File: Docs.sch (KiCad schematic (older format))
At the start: 0 parts

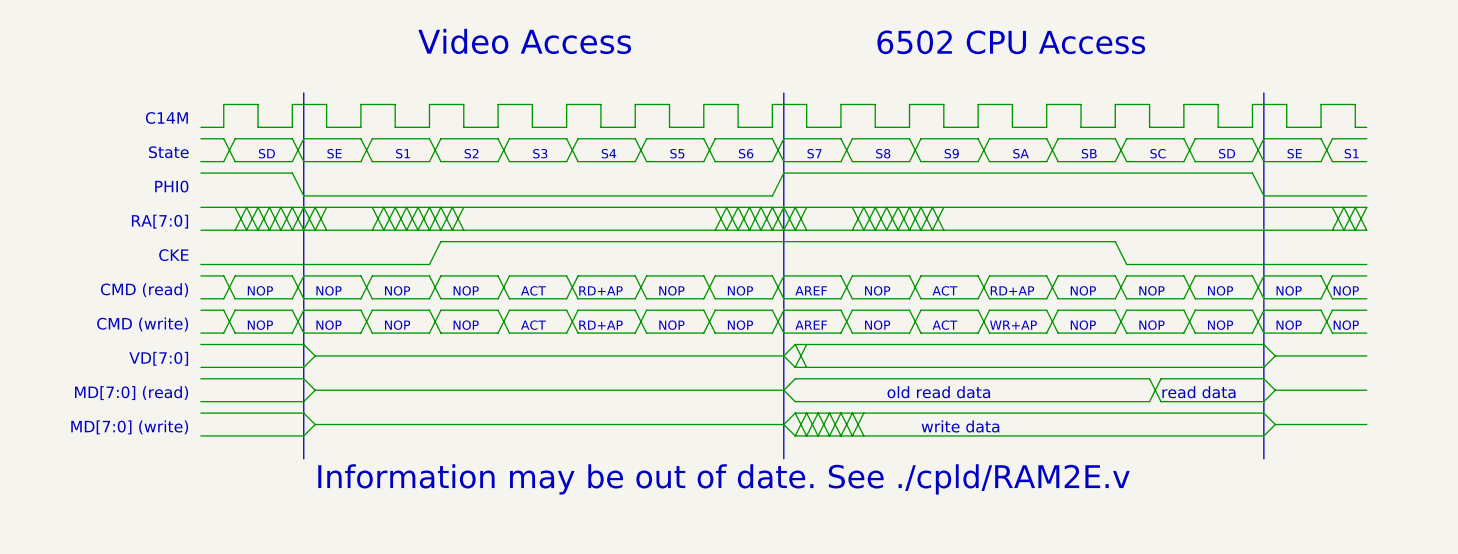
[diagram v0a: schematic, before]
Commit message: Added capacity selection
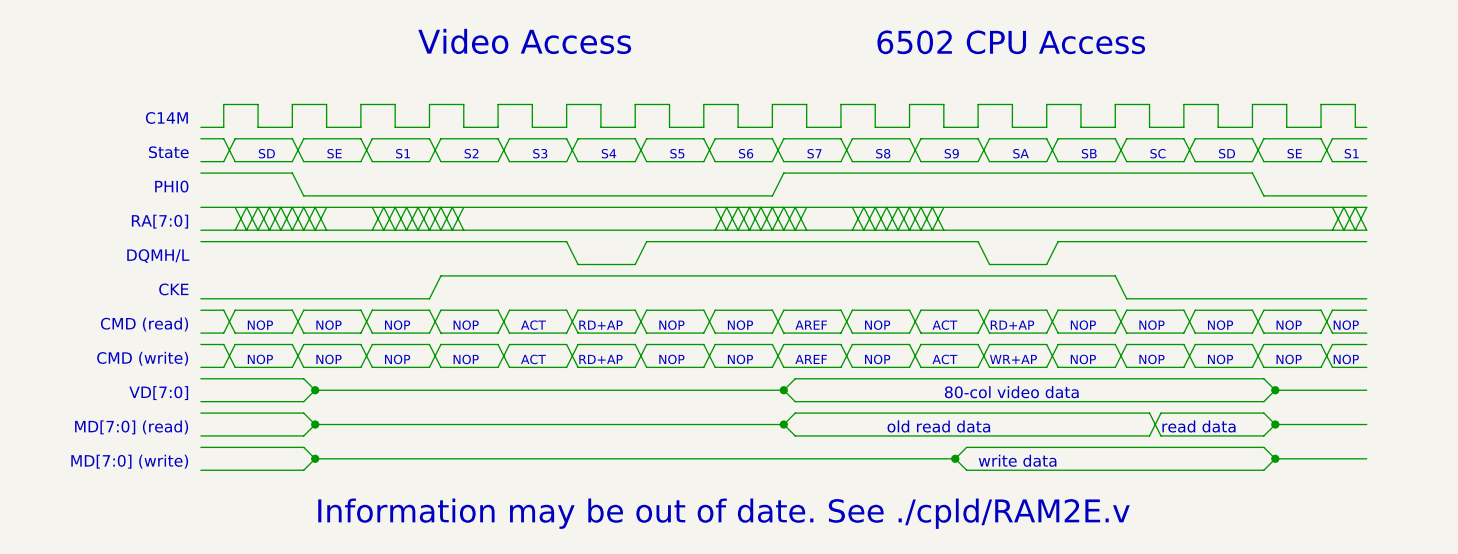
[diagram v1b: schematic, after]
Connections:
- wire segments 417 -> 412
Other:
- note added: "80-col video data"
- note added: "DQMH/L"

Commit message: Documentation update
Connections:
- wire segments 412 -> 411
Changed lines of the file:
@@
 Sheet 2 2
 Title "RAM2E II"
-Date "2020-05-06"
-Rev "0.9"
+Date "2020-07-25"
+Rev "1.0"
 Comp "Garrett's Workshop"
 Comment1 ""
@@
 Wire Wire Line
 	7350 2100 7400 2000
-Wire Wire Line
-	5600 2000 7050 2000
-Wire Wire Line
-	7400 2000 8750 2000
 Connection ~ 8350 2950
 Connection ~ 8350 2800
@@
 Text Notes 6900 2700 0    50   ~ 0
 80-col video data
+Wire Wire Line
+	5600 2000 8750 2000
 $EndSCHEMATC
